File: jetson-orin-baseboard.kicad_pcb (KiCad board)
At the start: 8 copper layers, 110 x 55 mm, 646 parts, among them IC1 ACPL-217-500E, J1 2199230-6, J10 533980471, J11 ERF8-040-05.0-L-DV-K-TR, J12 1053131102, J13 46756-1001, J2 1-2199230-6, J3 USB4105-GF-A, J4 WE_632723300011_alt_symbol, J5 WE_632723300011_alt_symbol, J6 5-2337992-8, J7 WE_68715014522, J8 WE_68715014522, J9 TC2050-IDC-NL, M1 jetson-orin-nx/nano-module, M2 M2_4222, M3 M2_2280, Q1 BSS138W-7-F, Q10 BSS138W-7-F, Q11 BSS138W-7-F, Q12 BSS138W-7-F, Q13 BCM857BS-7-F, Q14 BCM857BS-7-F, Q15 SSM3J332R, Q16 SSM3J332R, Q17 BSS138W-7-F, Q18 BSS138W-7-F, Q19 BSS138W-7-F, Q2 BSS138W-7-F, Q20 BSS138W-7-F, Q21 BSS138APW, Q3 BSS138W-7-F, Q4 BSS138W-7-F, Q5 BSS138W-7-F, Q6 BSS138W-7-F, Q7 BSS138W-7-F, Q8 BSS138W-7-F, Q9 BSS138W-7-F, SW1 PCM12SMTR, U1 74LVC1T45GM, U10 TUSB1046-DCI, U11 TPD4E05U06QDQARQ1, U12 AP22615, U13 TPD4E05U06QDQARQ1, U14 TPD4E05U06QDQARQ1, U15 TPD4E05U06QDQARQ1, U16 TPD4E05U06QDQARQ1, U17 HD3SS3220, U18 AP22615, U19 TPD4E05U06QDQARQ1, U2 74LVC2G07GV, U20 TPD4E05U06QDQARQ1, U21 TPD4E05U06QDQARQ1, U22 TPS2372-3RGWR, U23 ULS-12/5-D48N-C, U24 AP22615, U25 AP22615, U26 PCA9547BS, U27 NX3DV642, U28 NX3DV642, U29 AP22615, U3 74LVC2G07GV, U30 AP22615, U31 NTS0102GT, U32 NTS0102GT, U33 74LVC1T45GM, U34 PCAL6408ABSHP, U37 74LVC2G14GV, U38 74LVC1G175GV, U39 MP2386GG-P, U40 MP2386GG-P, U41 TPS7B8133DRVR, U42 TPS7A0518PDBVT, U43 NTS0102GT, U44 TPD4E02B04DQA, U45 TPD4E02B04DQA, U46 TPD4E02B04DQA, U5 FT230XQ-R, U6 TPS65988, U7 W25Q80DVUXIE_TR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

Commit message: Annotate parts, add them to PCB
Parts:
- removed C102, C103, C87, C88, C92, C93: C_100n_0402, antmicro-footprints:0402-cap
- removed the Q9 at (152.2, 191.6)
- removed TP1, TP34, TP35, TP44, TP45: TP_SMD_0_75MM, antmicro-footprints:Testpoint_smd_0_75mm
- removed U30: AP22615, antmicro-footprints:TSOT23-6
- added C40: C_100n_0402, antmicro-footprints:0402-cap, F.Cu at (207.1, 243.4)
- added C41: C_100n_0402, antmicro-footprints:0402-cap, F.Cu at (207.1, 241.4)
- added C42: C_100n_0402, antmicro-footprints:0402-cap, F.Cu at (151.1, 250.5)
- added C43: C_100n_0402, antmicro-footprints:0402-cap, F.Cu at (146.7, 258.5)
- added C44: C_100n_0402, antmicro-footprints:0402-cap, F.Cu at (181.0, 236.2)
- added C48: C_100n_0402, antmicro-footprints:0402-cap, F.Cu at (188.1, 236.2)
- added C49: C_1u_0402, antmicro-footprints:0402-cap, F.Cu at (236.4, 213.3)
- added C50: C_100n_0402, antmicro-footprints:0402-cap, F.Cu at (230.9, 218.3)
- added D39: TPD1E0B04DPYR, antmicro-footprints:XDFN-2_1x0.60mm, F.Cu at (181.3, 229.2)
- added D40: TPD1E0B04DPYR, antmicro-footprints:XDFN-2_1x0.60mm, F.Cu at (177.8, 230.5)
- added D41: TPD1E0B04DPYR, antmicro-footprints:XDFN-2_1x0.60mm, F.Cu at (188.4, 226.8)
- added D42: TPD1E0B04DPYR, antmicro-footprints:XDFN-2_1x0.60mm, F.Cu at (209.5, 219.4)
- added D43: TPD1E0B04DPYR, antmicro-footprints:XDFN-2_1x0.60mm, F.Cu at (192.0, 233.9)
- added D44: TPD1E0B04DPYR, antmicro-footprints:XDFN-2_1x0.60mm, F.Cu at (192.0, 226.4)
- added D45: TPD1E0B04DPYR, antmicro-footprints:XDFN-2_1x0.60mm, F.Cu at (177.8, 228.3)
- added D46: TPD1E0B04DPYR, antmicro-footprints:XDFN-2_1x0.60mm, F.Cu at (191.3, 224.3)
- added D47: TPD1E0B04DPYR, antmicro-footprints:XDFN-2_1x0.60mm, F.Cu at (184.2, 224.3)
- added D48: TPD1E0B04DPYR, antmicro-footprints:XDFN-2_1x0.60mm, F.Cu at (192.0, 231.7)
- added D49: TPD1E0B04DPYR, antmicro-footprints:XDFN-2_1x0.60mm, F.Cu at (188.4, 231.7)
- added D50: TPD1E0B04DPYR, antmicro-footprints:XDFN-2_1x0.60mm, F.Cu at (177.8, 235.1)
- added Q17: NX138BKMYL, antmicro-footprints:DFN1006-3, F.Cu at (233.5, 218.2)
- added Q18: SSM3J332R, antmicro-footprints:SOT-23-3, F.Cu at (232.6, 214.8)
- added R10: R_15k_0402, antmicro-footprints:0402-res, F.Cu at (151.1, 252.5)
- added R295: R_0R_0402, antmicro-footprints:0402-res, F.Cu at (146.7, 254.5)
- added R296: R_0R_0402, antmicro-footprints:0402-res, F.Cu at (140.9, 256.1)
- added R297: R_0R_0402, antmicro-footprints:0402-res, F.Cu at (146.7, 256.5)
- added R298: R_0R_0402, antmicro-footprints:0402-res, F.Cu at (156.9, 250.5)
- added R299: R_0R_0402, antmicro-footprints:0402-res, F.Cu at (145.3, 260.5)
- added R300: R_0R_0402, antmicro-footprints:0402-res, F.Cu at (149.6, 258.5)
- added R301: R_0R_0402, antmicro-footprints:0402-res, F.Cu at (140.9, 254.1)
- added R302: R_470R_0603, antmicro-footprints:0603-res, F.Cu at (181.3, 226.9)
- added R303: R_470R_0603, antmicro-footprints:0603-res, F.Cu at (187.8, 224.5)
- added R304: R_470R_0603, antmicro-footprints:0603-res, F.Cu at (188.4, 234.0)
- added R305: R_470R_0603, antmicro-footprints:0603-res, F.Cu at (192.0, 229.4)
- added R306: R_470R_0603, antmicro-footprints:0603-res, F.Cu at (181.3, 231.6)
- added R307: R_470R_0603, antmicro-footprints:0603-res, F.Cu at (195.6, 231.9)
- added R308: R_470R_0603, antmicro-footprints:0603-res, F.Cu at (195.6, 224.5)
- added R309: R_470R_0603, antmicro-footprints:0603-res, F.Cu at (184.9, 226.9)
- added R310: R_470R_0603, antmicro-footprints:0603-res, F.Cu at (195.6, 229.4)
- added R311: R_470R_0603, antmicro-footprints:0603-res, F.Cu at (202.7, 226.9)
- added R312: R_470R_0603, antmicro-footprints:0603-res, F.Cu at (199.1, 224.5)
- added R313: R_470R_0603, antmicro-footprints:0603-res, F.Cu at (184.9, 231.9)
- added R314: R_470R_0603, antmicro-footprints:0603-res, F.Cu at (180.7, 224.5)
- added R315: R_470R_0603, antmicro-footprints:0603-res, F.Cu at (206.2, 224.5)
- added R316: R_470R_0603, antmicro-footprints:0603-res, F.Cu at (195.6, 234.3)
- added R317: R_470R_0603, antmicro-footprints:0603-res, F.Cu at (184.9, 234.3)
- added R318: R_470R_0603, antmicro-footprints:0603-res, F.Cu at (216.6, 216.0)
- added R319: R_470R_0603, antmicro-footprints:0603-res, F.Cu at (195.6, 226.9)
- added R320: R_470R_0603, antmicro-footprints:0603-res, F.Cu at (216.0, 213.6)
- added R321: R_470R_0603, antmicro-footprints:0603-res, F.Cu at (202.7, 224.5)
- added R322: R_470R_0603, antmicro-footprints:0603-res, F.Cu at (177.8, 232.8)
- added R323: R_470R_0603, antmicro-footprints:0603-res, F.Cu at (199.1, 229.4)
- added R324: R_470R_0603, antmicro-footprints:0603-res, F.Cu at (213.0, 218.5)
- added R325: R_470R_0603, antmicro-footprints:0603-res, F.Cu at (209.5, 217.1)
- added R326: R_470R_0603, antmicro-footprints:0603-res, F.Cu at (199.1, 226.9)
- added R327: R_470R_0603, antmicro-footprints:0603-res, F.Cu at (199.1, 231.9)
- added R328: R_470R_0603, antmicro-footprints:0603-res, F.Cu at (199.1, 234.3)
- added R329: R_470R_0603, antmicro-footprints:0603-res, F.Cu at (192.0, 236.2)
- added R330: R_470R_0603, antmicro-footprints:0603-res, F.Cu at (209.5, 221.7)
- added R331: R_470R_0603, antmicro-footprints:0603-res, F.Cu at (188.4, 229.1)
- added R332: R_470R_0603, antmicro-footprints:0603-res, F.Cu at (184.9, 229.4)
- added R333: R_470R_0603, antmicro-footprints:0603-res, F.Cu at (181.3, 234.0)
- added R334: R_470R_0603, antmicro-footprints:0603-res, F.Cu at (212.5, 213.6)
- added R335: R_470R_0603, antmicro-footprints:0603-res, F.Cu at (202.7, 229.4)
- added R336: R_470R_0603, antmicro-footprints:0603-res, F.Cu at (213.0, 216.0)
- added R7: R_15k_0402, antmicro-footprints:0402-res, F.Cu at (145.2, 252.5)
- added R8: R_15k_0402, antmicro-footprints:0402-res, F.Cu at (143.8, 256.5)
- added R9: R_15k_0402, antmicro-footprints:0402-res, F.Cu at (149.6, 256.5)
- added REF**: 1053071202, antmicro-footprints:1053071202, F.Cu at (-5.90, 112.7)
- added U4: NTS0102GT, antmicro-footprints:PSON50P100X195X50-8N, F.Cu at (204.3, 242.2)
- J11: value ERF8-040-05.0-L-DV-K-TR -> LSHM-140-01-L-DH-A-S-TR; footprint antmicro-footprints:ERF8-040-XX.X-X-DV-XX -> antmicro-footprints:SAMTEC_LSHM-140-01-L-DH-A-S-TR; moved to B.Cu
- J7: moved to F.Cu
- Q1, Q2, Q3, Q4, Q5, Q6, Q7, Q8: value BSS138W-7-F -> NX138BKMYL; footprint antmicro-footprints:SOT-323 -> antmicro-footprints:DFN1006-3
- Q10: renamed from Q11; value BSS138W-7-F -> NX138BKMYL; footprint antmicro-footprints:SOT-323 -> antmicro-footprints:DFN1006-3
- Q11: renamed from Q12; value BSS138W-7-F -> NX138BKMYL; footprint antmicro-footprints:SOT-323 -> antmicro-footprints:DFN1006-3
- Q12: renamed from Q17; value BSS138W-7-F -> NX138BKMYL; footprint antmicro-footprints:SOT-323 -> antmicro-footprints:DFN1006-3
- Q19: renamed from Q18; value BSS138W-7-F -> NX138BKMYL; footprint antmicro-footprints:SOT-323 -> antmicro-footprints:DFN1006-3
- Q20: renamed from Q19; value BSS138W-7-F -> NX138BKMYL; footprint antmicro-footprints:SOT-323 -> antmicro-footprints:DFN1006-3
- Q21: renamed from Q20; value BSS138W-7-F -> NX138BKMYL; footprint antmicro-footprints:SOT-323 -> antmicro-footprints:DFN1006-3
- Q22: renamed from Q21; value BSS138APW -> NX138BKMYL; footprint antmicro-footprints:SC70-3 -> antmicro-footprints:DFN1006-3
- Q9: renamed from Q10; value BSS138W-7-F -> NX138BKMYL; footprint antmicro-footprints:SOT-323 -> antmicro-footprints:DFN1006-3
- R159: value R_100k_0402 -> R_4k7_0402
- R164, R165: value R_10k_0402 -> R_4k7_0402
- R175: value R_4k7_0402 -> R_0R_1206; footprint antmicro-footprints:0402-res -> antmicro-footprints:1206-res
- R176, R185, R186: value R_4k7_0402 -> R_0R_0402
- R183, R184, R220, R221: value R_10k_0402 -> R_0R_0402
- R187, R188, R189, R190: value R_49R9_0402 -> R_0R_0402
- R6: value R_10k_0402 -> R_100k_0402
- U24, U25: value AP22615 -> AP22653FDZ-7; footprint antmicro-footprints:TSOT23-6 -> antmicro-footprints:DFN-6-1EP_2x2mm_P0.65mm_EP1x1.6mm
- U27, U28: value NX3DV642 -> AP22653FDZ-7; footprint antmicro-footprints:QFN-24-1EP_3x4mm_P0.4mm_EP1.65x2.65mm -> antmicro-footprints:DFN-6-1EP_2x2mm_P0.65mm_EP1x1.6mm
- U29: value AP22615 -> TPD4E05U06QDQARQ1; footprint antmicro-footprints:TSOT23-6 -> antmicro-footprints:USON-10_2.5x1.0mm_P0.5mm
- U33: value 74LVC1T45GM -> NTS0102GT; footprint antmicro-footprints:SOT-886 -> antmicro-footprints:PSON50P100X195X50-8N
- moved R14 295.2 mm to (127.0, 101.0), turned to 180 degrees
- moved R28 294.4 mm to (127.0, 100.0), turned to 180 degrees
- moved C10 293.1 mm to (127.2, 98.0), turned to 180 degrees
- moved C9 292.4 mm to (127.2, 97.0), turned to 180 degrees
- moved R26 285.8 mm to (127.5, 86.0), turned to 90 degrees
- moved R25 283.9 mm to (126.5, 86.0), turned to 90 degrees
- moved J1 277.8 mm to (119.5, 96.4), turned to -90 degrees
- moved C12 276.5 mm to (114.9, 105.2), turned to 180 degrees
- moved R31 274.5 mm to (115.0, 102.7), turned to 180 degrees
- moved R30 273.6 mm to (115.0, 101.7), turned to 180 degrees
- moved R27 271.9 mm to (114.8, 99.8), turned to 0 degrees
- moved R35 269.1 mm to (115.0, 95.8), turned to 180 degrees
- moved R36 268.3 mm to (115.0, 94.8), turned to 180 degrees
- moved R33 267.5 mm to (115.0, 93.8), turned to 180 degrees
- moved R34 266.8 mm to (115.0, 92.8), turned to 180 degrees
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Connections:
- A1 pad 217: /SoM/MODULE_ID -> MODULE_ID
- A1 pad 236: DEBUG_TXD -> /SoM/DEBUG_TXD_1V8
- A1 pad 238: DEBUG_RXD -> /SoM/DEBUG_RXD_1V8
- J11 pad 27: PCIE2_RST* -> Net-(J11-Pad27)
- J11 pad 29: PCIE2_CLKREQ* -> Net-(J11-Pad29)
- J11 pad 30: PCIE3_RST* -> Net-(J11-Pad30)
- J11 pad 31: GPIO01 -> Net-(J11-Pad31)
- J11 pad 32: PCIE3_CLKREQ* -> Net-(J11-Pad32)
- J11 pad 33: GPIO07 -> Net-(J11-Pad33)
- J11 pad 34: PCIE_WAKE_SEL_EXT -> Net-(J11-Pad34)
- J11 pad 35: GPIO09 -> Net-(J11-Pad35)
- J11 pad 36: GPIO13 -> Net-(J11-Pad36)
- J11 pad 39: GPIO10 -> Net-(J11-Pad39)
- J11 pad 40: GPIO12 -> Net-(J11-Pad40)
- J11 pad 41: UART1_TXD -> Net-(J11-Pad41)
- J11 pad 42: GPIO11 -> Net-(J11-Pad42)
- J11 pad 43: UART1_RXD -> Net-(J11-Pad43)
- J11 pad 44: GPIO00 -> Net-(J11-Pad44)
- J11 pad 45: I2S0_SDIN -> Net-(J11-Pad45)
- J11 pad 46: I2S0_SCLK -> Net-(J11-Pad46)
- J11 pad 47: I2S0_LRCK -> Net-(J11-Pad47)
- J11 pad 48: I2S0_SDOUT -> Net-(J11-Pad48)
- J11 pad 51: SPIO_SCK -> Net-(J11-Pad51)
- J11 pad 52: SPI1_SCK -> Net-(J11-Pad52)
- J11 pad 53: SPIO_MOSI -> Net-(J11-Pad53)
- J11 pad 54: SPI1_MOSI -> Net-(J11-Pad54)
- J11 pad 55: SPIO_MISO -> Net-(J11-Pad55)
- J11 pad 56: SPI1_MISO -> Net-(J11-Pad56)
- J11 pad 57: ~{SPI0_CS0} -> Net-(J11-Pad57)
- J11 pad 58: ~{SPI1_CS0} -> Net-(J11-Pad58)
- J11 pad 59: ~{SPI0_CS1} -> Net-(J11-Pad59)
- J11 pad 60: ~{SPI1_CS1} -> Net-(J11-Pad60)
- J11 pad 63: SYS_SDA -> Net-(J11-Pad63)
- J11 pad 64: I2C2_SDA -> Net-(J11-Pad64)
- J11 pad 65: SYS_SCL -> Net-(J11-Pad65)
- J11 pad 66: I2C2_SCL -> Net-(J11-Pad66)
- J11 pad 68: CAN_RX -> Net-(J11-Pad68)
- J11 pad 70: CAN_TX -> Net-(J11-Pad70)
- Q13 pad 1: VCC -> /Supply/VCC_IN
- Q14 pad 1: VCC -> /Supply/VCC_IN
- Q15 pad 2: VCC -> /Supply/VCC_IN
- Q16 pad 2: VCC -> /Supply/VCC_IN
- R159 pad 1: GND -> MODULE_ID
- R159 pad 2: CSIA_PEN -> /Supply/VCC_IN
- R164 pad 1: /CSI/CSIA_5V_FLG -> Net-(C49-Pad2)
- R164 pad 2: +5V -> /Supply/VCC_IN
- R165 pad 1: /CSI/CSIA_3V3_FLG -> Net-(Q17-Pad3)
- R165 pad 2: +3V3 -> Net-(C49-Pad2)
- R175 pad 1: GND -> /Supply/VCC_IN
- R175 pad 2: /CSI/CSIA_5V_ISET -> VCC
- R176 pad 1: GND -> CSI1_CLK_P
- R176 pad 2: /CSI/CSIA_3V3_ISET -> /CSI/CSI1_1_CLK_P
- R181 pad 1: GND -> CSI1_CLK_N
- R181 pad 2: /CSI/~{CSI_MUX1_OE} -> /CSI/CSI1_1_CLK_N
- R182 pad 1: GND -> CSI1_D0_P
- R182 pad 2: /CSI/~{CSI_MUX0_OE} -> /CSI/CSI1_1_D0_P
- R183 pad 1: /CSI/CSIB_5V_FLG -> CSI1_D0_N
- R183 pad 2: +5V -> /CSI/CSI1_1_D0_N
- R184 pad 1: /CSI/CSIB_3V3_FLG -> CSI1_D1_P
- R184 pad 2: +3V3 -> /CSI/CSI1_1_D1_P
- R185 pad 1: GND -> CSI1_D1_N
- R185 pad 2: /CSI/CSIB_5V_ISET -> /CSI/CSI1_1_D1_N
- R186 pad 1: GND -> CSI1_D1_P
- R186 pad 2: /CSI/CSIB_3V3_ISET -> /CSI/CSI1_0_D0_P
- R187 pad 1: /CSI/CSI1_0_CLK_P -> CSI1_D1_N
- R187 pad 2: GND -> /CSI/CSI1_0_D0_N
- R188 pad 1: /CSI/CSI1_0_CLK_N -> CSI1_D0_P
- R188 pad 2: GND -> /CSI/CSI1_0_D1_P
- R189 pad 1: /CSI/CSI3_0_CLK_P -> CSI1_D0_N
- R189 pad 2: GND -> /CSI/CSI1_0_D1_N
- R190 pad 1: /CSI/CSI3_0_CLK_N -> CSI3_CLK_P
- R190 pad 2: GND -> /CSI/CSI3_1_CLK_P
- R220 pad 1: FAN_TACH -> CSI3_CLK_N
- R220 pad 2: +1V8 -> /CSI/CSI3_1_CLK_N
- R221 pad 1: /Peripherals/FAN_TACH_5V -> CSI3_D0_P
- R221 pad 2: +5V -> /CSI/CSI3_1_D0_P
- R252 pad 2: VCC -> /Supply/VCC_IN
- R253 pad 2: VCC -> /Supply/VCC_IN
- R6 pad 1: /SoM/MODULE_ID -> GND
- R6 pad 2: 3V3_STDB -> CSIA_PEN
- U24 pad 2: GND -> /CSI/CSIA_5V_ISET
- U24 pad 3: /CSI/CSIA_5V_FLG -> unconnected-(U24-Pad3)
- U24 pad 5: /CSI/CSIA_5V_ISET -> GND
- U25 pad 2: GND -> /CSI/CSIA_3V3_ISET
- U25 pad 3: /CSI/CSIA_3V3_FLG -> unconnected-(U25-Pad3)
- U25 pad 5: /CSI/CSIA_3V3_ISET -> GND
- U27 pad 1: CSI1_CLK_P -> /CSI/CSIB_5V
- U27 pad 2: CSI1_CLK_N -> /CSI/CSIB_5V_ISET
- U27 pad 3: CSI1_D0_P -> unconnected-(U27-Pad3)
- U27 pad 4: CSI1_D0_N -> CSIB_PEN
- U27 pad 5: CSI1_D1_P -> GND
- U27 pad 6: CSI1_D1_N -> +5V
- U28 pad 1: CSI3_CLK_P -> /CSI/CSIB_3V3
- U28 pad 2: CSI3_CLK_N -> /CSI/CSIB_3V3_ISET
- U28 pad 3: CSI3_D0_P -> unconnected-(U28-Pad3)
- U28 pad 4: CSI3_D0_N -> CSIB_PEN
- U28 pad 5: CSI3_D1_P -> GND
- U28 pad 6: CSI3_D1_N -> +3V3
- U29 pad 1: /CSI/CSIB_5V -> /Peripherals/USBSS2_RX_CONN_N
- U29 pad 2: GND -> /Peripherals/USBSS2_RX_CONN_P
- U29 pad 3: /CSI/CSIB_5V_FLG -> GND
- U29 pad 4: CSIB_PEN -> /Peripherals/USBSS2_TX_CONN_N
- U29 pad 5: /CSI/CSIB_5V_ISET -> /Peripherals/USBSS2_TX_CONN_P
- U29 pad 6: +5V -> /Peripherals/USBSS2_TX_CONN_P
- U33 pad 1: +1V8 -> /Peripherals/FAN_TACH_5V
- U33 pad 3: FAN_PWM -> +1V8
- U33 pad 4: /Peripherals/FAN_PWM_5V -> FAN_TACH
- U33 pad 5: +1V8 -> FAN_PWM
- U33 pad 6: +5V -> +1V8

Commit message: Change power connector to SMD
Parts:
- removed R228, R229: R_0R_0402, antmicro-footprints:0402-res
- removed the REF** at (-5.90, 112.7)
- added J13: 46756-1001, antmicro-footprints:HDMI-micro-D-cable-end, F.Cu at (94.2, 125.5)
- added J4: WE_632723300011_alt_symbol, antmicro-footprints:USB-type-C-cable-end, F.Cu at (75.0, 125.8)
- added J4: WE_632723300011_alt_symbol, antmicro-footprints:USB-type-C-cable-end, F.Cu at (113.7, 125.8)
- added REF**: 1053071202, antmicro-footprints:Molex-NanoFit-plug-end, F.Cu at (53.3, 114.4)
- added TP1: TP_SMD_0_75MM, antmicro-footprints:Testpoint_smd_0_75mm, F.Cu at (-205.6, 87.6)
- added TP34: TP_SMD_0_75MM, antmicro-footprints:Testpoint_smd_0_75mm, F.Cu at (-205.6, 89.4)
- J12: value 1053131102 -> Molex_Nano-Fit-105430_xx02-horizontal; footprint antmicro-footprints:1053131102 -> antmicro-footprints:Molex_Nano-Fit_105430-xx02_1x02_P2.50mm_Horizontal_SMD
- moved R190 214.0 mm to (-70.0, 234.6)
- moved C105 214.0 mm to (-61.0, 83.7)
- moved C106 214.0 mm to (-61.0, 85.7)
- moved C107 214.0 mm to (-61.0, 88.2)
- moved C108 214.0 mm to (-61.6, 59.6)
- moved C112 214.0 mm to (-61.6, 60.6)
- moved C116 214.0 mm to (-100.7, 145.4)
- moved C117 214.0 mm to (-101.2, 146.9)
- moved C118 214.0 mm to (-94.7, 145.8)
- moved C119 214.0 mm to (-93.2, 145.3)
- moved C121 214.0 mm to (-165.1, 129.3)
- moved C123 214.0 mm to (-165.1, 133.2)
- moved C124 214.0 mm to (-84.7, 145.8)
- moved C126 214.0 mm to (-163.1, 133.2)
- moved C127 214.0 mm to (-164.1, 148.1)
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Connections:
- J4 pad A1: GND -> (no net)
- J4 pad A10: /USB Debug, DP/USBC0_CONN_RX2_N -> (no net)
- J4 pad A11: /USB Debug, DP/USBC0_CONN_RX2_P -> (no net)
- J4 pad A12: GND -> (no net)
- J4 pad A2: /USB Debug, DP/USBC0_CONN_TX1_P -> (no net)
- J4 pad A3: /USB Debug, DP/USBC0_CONN_TX1_N -> (no net)
- J4 pad A4: /USB Debug, DP/USBC0_VBUS -> (no net)
- J4 pad A5: /USB Debug, DP/USBC0_CC1 -> (no net)
- J4 pad A6: Net-(J4-PadA6) -> (no net)
- J4 pad A7: Net-(J4-PadA7) -> (no net)
- J4 pad A8: /USB Debug, DP/USBC0_SBU1 -> (no net)
- J4 pad A9: /USB Debug, DP/USBC0_VBUS -> (no net)
- J4 pad B1: GND -> (no net)
- J4 pad B10: /USB Debug, DP/USBC0_CONN_RX1_N -> (no net)
- J4 pad B11: /USB Debug, DP/USBC0_CONN_RX1_P -> (no net)
- J4 pad B12: GND -> (no net)
- J4 pad B2: /USB Debug, DP/USBC0_CONN_TX2_P -> (no net)
- J4 pad B3: /USB Debug, DP/USBC0_CONN_TX2_N -> (no net)
- J4 pad B4: /USB Debug, DP/USBC0_VBUS -> (no net)
- J4 pad B5: /USB Debug, DP/USBC0_CC2 -> (no net)
- J4 pad B6: Net-(J4-PadA6) -> (no net)
- J4 pad B7: Net-(J4-PadA7) -> (no net)
- J4 pad B8: /USB Debug, DP/USBC0_SBU2 -> (no net)
- J4 pad B9: /USB Debug, DP/USBC0_VBUS -> (no net)
- J4 pad Shell: GND -> (no net)
- R224 pad 2: CSI1_SW -> CSIA_PEN
- R225 pad 2: CSI3_SW -> CSIB_PEN
- R226 pad 2: CSIA_PEN -> USBC1_PEN
- R227 pad 2: CSIB_PEN -> DISABLE_POE_DCDC
- U34 pad 7: /Peripherals/GPIOEX_P0_4 -> Net-(U34-Pad7)
- U34 pad 8: /Peripherals/GPIOEX_P0_6 -> Net-(U34-Pad8)

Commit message: Remove R0s from high speed signals, replace part of R0s with resistor ladder. Assign net clases
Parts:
- removed R100, R101, R102, R103, R107, R108, R120, R121, R122, R123, R129, R130, R131, R132, R133, R134, R199, R200, R201, R202, R207, R208, R209, R210, R36, R48, R50, R51, R52, R53, R54, R55, R62, R63, R64: R_0R_0402, antmicro-footprints:0402-res
- R21, R22, R23, R24, R33, R34, R35: value R_0R_0402 -> 4x0R_0201_array; footprint antmicro-footprints:0402-res -> antmicro-footprints:EXB18V
- moved R23 319.4 mm to (-200.0, 142.2)
- moved R24 313.3 mm to (-194.0, 142.3), turned to 180 degrees
- moved R33 305.7 mm to (-185.1, 151.6)
- moved R34 57.7 mm to (81.2, 139.5), turned to 0 degrees
- moved R35 53.5 mm to (84.4, 139.5), turned to 0 degrees
- moved R22 6.35 mm to (114.8, 95.1)
- moved R21 1.87 mm to (114.8, 89.6)
- turned U19 to 90 degrees
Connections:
- J4 pad A1: (no net) -> GND
- J4 pad A10: (no net) -> /USB Debug, DP/USBC0_CONN_RX2_N
- J4 pad A11: (no net) -> /USB Debug, DP/USBC0_CONN_RX2_P
- J4 pad A12: (no net) -> GND
- J4 pad A2: (no net) -> /USB Debug, DP/USBC0_CONN_TX1_P
- J4 pad A3: (no net) -> /USB Debug, DP/USBC0_CONN_TX1_N
- J4 pad A4: (no net) -> /USB Debug, DP/USBC0_VBUS
- J4 pad A5: (no net) -> /USB Debug, DP/USBC0_CC1
- J4 pad A6: (no net) -> USB0_D_P
- J4 pad A7: (no net) -> USB0_D_N
- J4 pad A8: (no net) -> /USB Debug, DP/USBC0_SBU1
- J4 pad A9: (no net) -> /USB Debug, DP/USBC0_VBUS
- J4 pad B1: (no net) -> GND
- J4 pad B10: (no net) -> /USB Debug, DP/USBC0_RX1_N
- J4 pad B11: (no net) -> /USB Debug, DP/USBC0_RX1_P
- J4 pad B12: (no net) -> GND
- J4 pad B2: (no net) -> /USB Debug, DP/USBC0_CONN_TX2_P
- J4 pad B3: (no net) -> /USB Debug, DP/USBC0_CONN_TX2_N
- J4 pad B4: (no net) -> /USB Debug, DP/USBC0_VBUS
- J4 pad B5: (no net) -> /USB Debug, DP/USBC0_CC2
- J4 pad B6: (no net) -> USB0_D_P
- J4 pad B7: (no net) -> USB0_D_N
- J4 pad B8: (no net) -> /USB Debug, DP/USBC0_SBU2
- J4 pad B9: (no net) -> /USB Debug, DP/USBC0_VBUS
- J4 pad Shell: (no net) -> GND
- J5 pad A10: /USB3/USBC1_CONN_RX2_N -> /USB3/USBC1_RX2_N
- J5 pad A11: /USB3/USBC1_CONN_RX2_P -> /USB3/USBC1_RX2_P
- J5 pad A6: /USB3/USBC1_CONN_D_P -> USB1_D_P
- J5 pad A7: /USB3/USBC1_CONN_D_N -> USB1_D_N
- J5 pad B10: /USB3/USBC1_CONN_RX1_N -> /USB3/USBC1_RX1_N
- J5 pad B11: /USB3/USBC1_CONN_RX1_P -> /USB3/USBC1_RX1_P
- J5 pad B6: /USB3/USBC1_CONN_D_P -> USB1_D_P
- J5 pad B7: /USB3/USBC1_CONN_D_N -> USB1_D_N
- R21 pad 2: /M.2/M2_E_PCM_CLK -> I2S1_LRCK
- R22 pad 1: I2S1_LRCK -> UART0_RXD
- R22 pad 2: /M.2/M2_E_PCM_SYNC -> UART0_TXD
- R23 pad 1: I2S1_SDOUT -> PDC_MOSI
- R23 pad 2: /M.2/M2_E_PCM_OUT -> PDC_SCLK
- R24 pad 1: I2S1_SDIN -> EEPROM_PWR
- R24 pad 2: /M.2/M2_E_PCM_in -> PDC_MISO
- R33 pad 1: /M.2/M2_E_UART_RX -> unconnected-(R33-Pad1)
- R33 pad 2: UART0_TXD -> /USB Debug, DP/PDC_CTL1
- R34 pad 1: /M.2/M2_E_UART_TX -> /CSI/SDA_CAM0
- R34 pad 2: UART0_RXD -> /CSI/SCL_CAM0
- R35 pad 1: /M.2/M2_E_UART_CTS -> /CSI/SDA_CAM2
- R35 pad 2: UART0_CTS -> /CSI/SCL_CAM2
- U10 pad 39: /USB Debug, DP/USBC0_RX2_N -> /USB Debug, DP/USBC0_CONN_RX2_N
- U10 pad 40: /USB Debug, DP/USBC0_RX2_P -> /USB Debug, DP/USBC0_CONN_RX2_P
- U15 pad 1: /USB Debug, DP/USBC0_CONN_RX1_N -> /USB Debug, DP/USBC0_RX1_N
- U15 pad 10: /USB Debug, DP/USBC0_CONN_RX1_N -> /USB Debug, DP/USBC0_RX1_N
- U15 pad 2: /USB Debug, DP/USBC0_CONN_RX1_P -> /USB Debug, DP/USBC0_RX1_P
- U15 pad 9: /USB Debug, DP/USBC0_CONN_RX1_P -> /USB Debug, DP/USBC0_RX1_P
- U16 pad 1: Net-(J4-PadA6) -> USB0_D_P
- U16 pad 10: Net-(J4-PadA6) -> USB0_D_P
- U16 pad 2: Net-(J4-PadA7) -> USB0_D_N
- U16 pad 9: Net-(J4-PadA7) -> USB0_D_N
- U17 pad 10: /USB3/USBSS1_RX_C_N -> USBSS1_RX_N
- U17 pad 6: /USB3/USBSS1_TX_C_P -> USBSS1_TX_P
- U17 pad 7: /USB3/USBSS1_TX_C_N -> USBSS1_TX_N
- U17 pad 9: /USB3/USBSS1_RX_C_P -> USBSS1_RX_P
- U19 pad 1: /USB3/USBC1_CONN_RX2_N -> /USB3/USBC1_RX2_N
- U19 pad 10: /USB3/USBC1_CONN_RX2_N -> /USB3/USBC1_RX2_N
- U19 pad 2: /USB3/USBC1_CONN_RX2_P -> /USB3/USBC1_RX2_P
- U19 pad 9: /USB3/USBC1_CONN_RX2_P -> /USB3/USBC1_RX2_P
- U20 pad 1: /USB3/USBC1_CONN_RX1_N -> /USB3/USBC1_RX1_N
- U20 pad 10: /USB3/USBC1_CONN_RX1_N -> /USB3/USBC1_RX1_N
- U20 pad 2: /USB3/USBC1_CONN_RX1_P -> /USB3/USBC1_RX1_P
- U20 pad 9: /USB3/USBC1_CONN_RX1_P -> /USB3/USBC1_RX1_P
- U21 pad 1: /USB3/USBC1_CONN_D_P -> USB1_D_P
- U21 pad 10: /USB3/USBC1_CONN_D_P -> USB1_D_P
- U21 pad 2: /USB3/USBC1_CONN_D_N -> USB1_D_N
- U21 pad 9: /USB3/USBC1_CONN_D_N -> USB1_D_N
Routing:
- net USBSS1_RX_P: track 0.00 -> 3.00 mm, vias 0 -> 1
- net USBSS1_RX_N: track 0.00 -> 2.90 mm, vias 0 -> 1

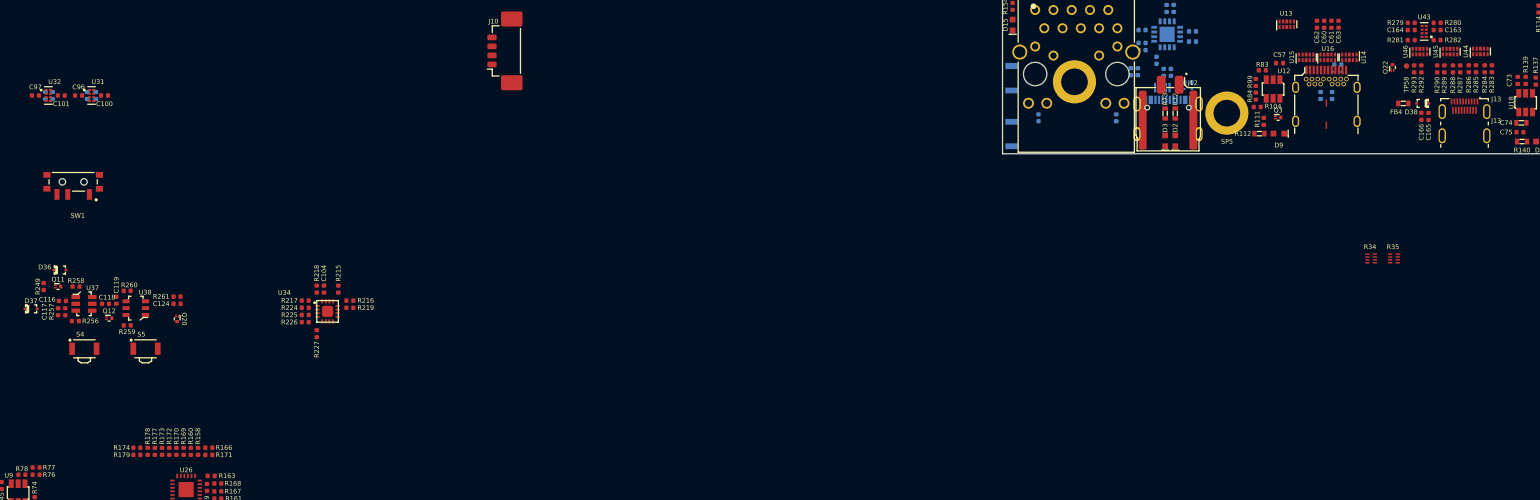
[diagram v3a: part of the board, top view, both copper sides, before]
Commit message: Minor cleanup, annotate parts, import them to PCB
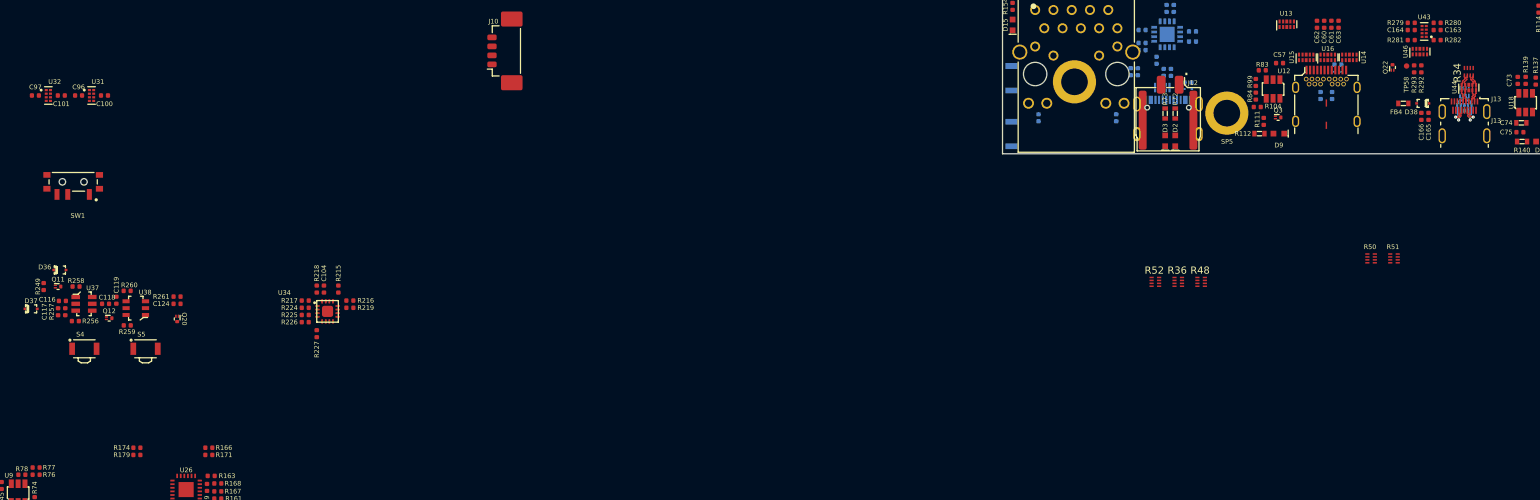
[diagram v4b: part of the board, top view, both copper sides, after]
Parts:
- removed R158, R160, R169, R170, R172, R173, R177, R178: R_2k2_0402, antmicro-footprints:0402-res
- removed R211, R212, R213, R214, R283, R284, R285, R286, R287, R288, R289, R290: R_0R_0402, antmicro-footprints:0402-res
- added R34: 4x0R_0201_array, antmicro-footprints:EXB18V, F.Cu at (94.8, 113.6)
- added R35: 4x0R_0201_array, antmicro-footprints:EXB18V, B.Cu at (94.2, 116.4)
- added R36: 4x2k2_0201_array, antmicro-footprints:EXB18V, F.Cu at (54.4, 142.8)
- added R48: 4x2k2_0201_array, antmicro-footprints:EXB18V, F.Cu at (57.6, 142.8)
- added R52: 4x2k2_0201_array, antmicro-footprints:EXB18V, F.Cu at (51.2, 142.8)
- U45: moved to B.Cu
- moved U45 8.06 mm to (94.2, 118.6), turned to -90 degrees
- moved U44 5.26 mm to (94.8, 115.8)
- renumbered R34 to R50, R35 to R51
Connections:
- net /USB Debug, DP/USBC0_RX1_N renamed /USB Debug, DP/USBC0_CONN_RX1_N
- net /USB Debug, DP/USBC0_RX1_P renamed /USB Debug, DP/USBC0_CONN_RX1_P
- net /USB Debug, DP/USBC3_D_P renamed Net-(J3-PadA6)
- D4 pad 2: GND -> unconnected-(D4-Pad2)
- D5 pad 2: GND -> unconnected-(D5-Pad2)
- U44 pad 1: /HDMI/HDMI_D1_N -> /HDMI/HDMI_D0_CONN_N
- U44 pad 10: /HDMI/HDMI_D1_N -> /HDMI/HDMI_D0_CONN_N
- U44 pad 2: /HDMI/HDMI_D1_P -> /HDMI/HDMI_D0_CONN_P
- U44 pad 4: /HDMI/HDMI_D2_N -> /HDMI/HDMI_D2_CONN_N
- U44 pad 5: /HDMI/HDMI_D2_P -> /HDMI/HDMI_D2_CONN_P
- U44 pad 6: /HDMI/HDMI_D2_P -> /HDMI/HDMI_D2_CONN_P
- U44 pad 7: /HDMI/HDMI_D2_N -> /HDMI/HDMI_D2_CONN_N
- U44 pad 9: /HDMI/HDMI_D1_P -> /HDMI/HDMI_D0_CONN_P
- U45 pad 1: /HDMI/HDMI_CLK_N -> /HDMI/HDMI_CLK_CONN_N
- U45 pad 10: /HDMI/HDMI_CLK_N -> /HDMI/HDMI_CLK_CONN_N
- U45 pad 2: /HDMI/HDMI_CLK_P -> /HDMI/HDMI_CLK_CONN_P
- U45 pad 4: /HDMI/HDMI_D0_N -> /HDMI/HDMI_D1_CONN_N
- U45 pad 5: /HDMI/HDMI_D0_P -> /HDMI/HDMI_D1_CONN_P
- U45 pad 6: /HDMI/HDMI_D0_P -> /HDMI/HDMI_D1_CONN_P
- U45 pad 7: /HDMI/HDMI_D0_N -> /HDMI/HDMI_D1_CONN_N
- U45 pad 9: /HDMI/HDMI_CLK_P -> /HDMI/HDMI_CLK_CONN_P
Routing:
- net /HDMI/HDMI_CLK_CONN_P: track 0.00 -> 5.47 mm, vias 0 -> 1
- net /HDMI/HDMI_D1_CONN_N: track 0.00 -> 5.24 mm, vias 0 -> 1
- net /HDMI/HDMI_CLK_CONN_N: track 0.00 -> 5.16 mm, vias 0 -> 1
- net /HDMI/HDMI_D1_CONN_P: track 0.00 -> 4.82 mm, vias 0 -> 1
- net /HDMI/HDMI_D2_CONN_N: track 0.00 -> 4.10 mm
- net /HDMI/HDMI_D2_CONN_P: track 0.00 -> 4.10 mm
- net /HDMI/HDMI_D0_CONN_P: track 0.00 -> 3.97 mm
- net /HDMI/HDMI_D0_CONN_N: track 0.00 -> 3.97 mm
